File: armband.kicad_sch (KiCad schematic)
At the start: 14 parts, among them IC1 QSMP-1570, SW1 EVP-BB2A9B000, SW2 EVP-BB2A9B000

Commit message: progressed layout
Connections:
- net BMI_INT1: now also IC1.24 (ENET_RXC); no longer IC1.20 (ENET_CK125)
- net BMI_INT2: now also IC1.25 (ENET_RX_CTL); no longer IC1.21 (ENET_INT)
- net LCD_RST: now also IC1.20 (ENET_CK125); no longer IC1.26 (ENET_RXD0)
- net LCD_TE: now also IC1.19 (ENET_RST); no longer IC1.25 (ENET_RX_CTL)
- net MAX_INT: now also IC1.26 (ENET_RXD0); no longer IC1.22 (ENET_MDIO)
- net MP2722_INT: now also IC1.27 (ENET_RXD1); no longer IC1.19 (ENET_RST)
- net QSMP_LCD_EN: now also IC1.23 (ENET_MDC); no longer IC1.27 (ENET_RXD1)
- net TP_INT: now also IC1.21 (ENET_INT); no longer IC1.23 (ENET_MDC)
- net TP_RST: now also IC1.22 (ENET_MDIO); no longer IC1.24 (ENET_RXC)
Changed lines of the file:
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@@
     )
   )
-  (global_label "BMI_INT2" (shape input) (at 236.22 139.7 0) (fields_autoplaced)
-    (effects (font (size 1.27 1.27)) (justify left))
-    (property "Intersheetrefs" "${INTERSHEET_REFS}" (at 247.532 139.7 0)
+  (global_label "BMI_INT2" (shape input) (at 236.22 149.86 0) (fields_autoplaced)
+    (effects (font (size 1.27 1.27)) (justify left))
+    (property "Intersheetrefs" "${INTERSHEET_REFS}" (at 247.532 149.86 0)
       (effects (font (size 1.27 1.27)) (justify left) hide)
     )
@@
     )
   )
-  (global_label "TP_RST" (shape input) (at 236.22 147.32 0) (fields_autoplaced)
-    (effects (font (size 1.27 1.27)) (justify left))
-    (property "Intersheetrefs" "${INTERSHEET_REFS}" (at 245.7781 147.32 0)
+  (global_label "TP_RST" (shape input) (at 236.22 142.24 0) (fields_autoplaced)
+    (effects (font (size 1.27 1.27)) (justify left))
+    (property "Intersheetrefs" "${INTERSHEET_REFS}" (at 245.7781 142.24 0)
       (effects (font (size 1.27 1.27)) (justify left) hide)
     )
@@
     )
   )
-  (global_label "QSMP_LCD_EN" (shape input) (at 236.22 154.94 0) (fields_autoplaced)
-    (effects (font (size 1.27 1.27)) (justify left))
-    (property "Intersheetrefs" "${INTERSHEET_REFS}" (at 252.37 154.94 0)
+  (global_label "QSMP_LCD_EN" (shape input) (at 236.22 144.78 0) (fields_autoplaced)
+    (effects (font (size 1.27 1.27)) (justify left))
+    (property "Intersheetrefs" "${INTERSHEET_REFS}" (at 252.37 144.78 0)
       (effects (font (size 1.27 1.27)) (justify left) hide)
     )
@@
     )
   )
-  (global_label "MP2722_INT" (shape input) (at 236.22 134.62 0) (fields_autoplaced)
-    (effects (font (size 1.27 1.27)) (justify left))
-    (property "Intersheetrefs" "${INTERSHEET_REFS}" (at 250.5557 134.62 0)
+  (global_label "MP2722_INT" (shape input) (at 236.22 154.94 0) (fields_autoplaced)
+    (effects (font (size 1.27 1.27)) (justify left))
+    (property "Intersheetrefs" "${INTERSHEET_REFS}" (at 250.5557 154.94 0)
       (effects (font (size 1.27 1.27)) (justify left) hide)
     )
@@
     )
   )
-  (global_label "MAX_INT" (shape input) (at 236.22 142.24 0) (fields_autoplaced)
-    (effects (font (size 1.27 1.27)) (justify left))
-    (property "Intersheetrefs" "${INTERSHEET_REFS}" (at 246.7458 142.24 0)
+  (global_label "MAX_INT" (shape input) (at 236.22 152.4 0) (fields_autoplaced)
+    (effects (font (size 1.27 1.27)) (justify left))
+    (property "Intersheetrefs" "${INTERSHEET_REFS}" (at 246.7458 152.4 0)
       (effects (font (size 1.27 1.27)) (justify left) hide)
     )
@@
     )
   )
-  (global_label "BMI_INT1" (shape input) (at 236.22 137.16 0) (fields_autoplaced)
-    (effects (font (size 1.27 1.27)) (justify left))
-    (property "Intersheetrefs" "${INTERSHEET_REFS}" (at 247.532 137.16 0)
+  (global_label "BMI_INT1" (shape input) (at 236.22 147.32 0) (fields_autoplaced)
+    (effects (font (size 1.27 1.27)) (justify left))
+    (property "Intersheetrefs" "${INTERSHEET_REFS}" (at 247.532 147.32 0)
       (effects (font (size 1.27 1.27)) (justify left) hide)
     )
@@
     )
   )
-  (global_label "LCD_TE" (shape input) (at 236.22 149.86 0) (fields_autoplaced)
-    (effects (font (size 1.27 1.27)) (justify left))
-    (property "Intersheetrefs" "${INTERSHEET_REFS}" (at 245.7781 149.86 0)
+  (global_label "LCD_TE" (shape input) (at 236.22 134.62 0) (fields_autoplaced)
+    (effects (font (size 1.27 1.27)) (justify left))
+    (property "Intersheetrefs" "${INTERSHEET_REFS}" (at 245.7781 134.62 0)
       (effects (font (size 1.27 1.27)) (justify left) hide)
     )
@@
     )
   )
-  (global_label "LCD_RST" (shape input) (at 236.22 152.4 0) (fields_autoplaced)
-    (effects (font (size 1.27 1.27)) (justify left))
-    (property "Intersheetrefs" "${INTERSHEET_REFS}" (at 247.1086 152.4 0)
+  (global_label "LCD_RST" (shape input) (at 236.22 137.16 0) (fields_autoplaced)
+    (effects (font (size 1.27 1.27)) (justify left))
+    (property "Intersheetrefs" "${INTERSHEET_REFS}" (at 247.1086 137.16 0)
       (effects (font (size 1.27 1.27)) (justify left) hide)
     )
@@
     )
   )
-  (global_label "TP_INT" (shape input) (at 236.22 144.78 0) (fields_autoplaced)
-    (effects (font (size 1.27 1.27)) (justify left))
-    (property "Intersheetrefs" "${INTERSHEET_REFS}" (at 245.2339 144.78 0)
-      (effects (font (size 1.27 1.27)) (justify left) hide)
-    )
+  (global_label "TP_INT" (shape input) (at 236.22 139.7 0) (fields_autoplaced)
+    (effects (font (size 1.27 1.27)) (justify left))
+    (property "Intersheetrefs" "${INTERSHEET_REFS}" (at 245.2339 139.7 0)
+      (effects (font (size 1.27 1.27)) (justify left) hide)
+    )

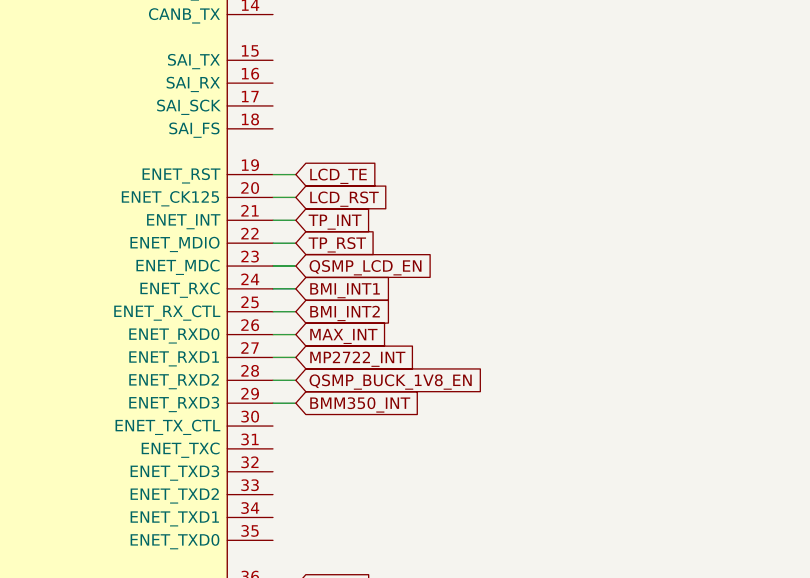
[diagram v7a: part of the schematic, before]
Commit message: progressed layout and made changes in bmi323 (set unconnected pins to NC) + changed debug connections in preparation to make bridges to debug part + changed VSYS, VUSB, VBAT+ and other connected power traces to 0.2mm trace thickness + added BMI323 layout + moved MAX30102 to make space for caps + added missing caps to MAX30102 + changed gpio order for better layout + added BMM350 layout next to BMI323
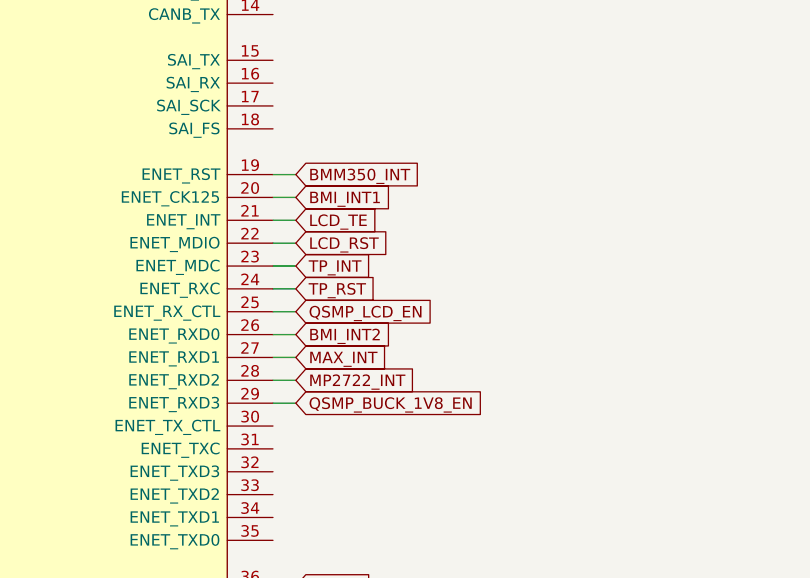
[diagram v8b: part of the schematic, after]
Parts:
- R1, R2, R3, R4: footprint Resistor_SMD:R_0201_0603Metric_Pad0.64x0.40mm_HandSolder -> Resistor_SMD:R_0201_0603Metric
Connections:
- net BMI_INT1: now also IC1.20 (ENET_CK125); no longer IC1.24 (ENET_RXC)
- net BMI_INT2: now also IC1.26 (ENET_RXD0); no longer IC1.25 (ENET_RX_CTL)
- net BMM350_INT: now also IC1.19 (ENET_RST); no longer IC1.29 (ENET_RXD3)
- net LCD_RST: now also IC1.22 (ENET_MDIO); no longer IC1.20 (ENET_CK125)
- net LCD_TE: now also IC1.21 (ENET_INT); no longer IC1.19 (ENET_RST)
- net MAX_INT: now also IC1.27 (ENET_RXD1); no longer IC1.26 (ENET_RXD0)
- net MP2722_INT: now also IC1.28 (ENET_RXD2); no longer IC1.27 (ENET_RXD1)
- net QSMP_BUCK_1V8_EN: now also IC1.29 (ENET_RXD3); no longer IC1.28 (ENET_RXD2)
- net QSMP_LCD_EN: now also IC1.25 (ENET_RX_CTL); no longer IC1.23 (ENET_MDC)
- net TP_INT: now also IC1.23 (ENET_MDC); no longer IC1.21 (ENET_INT)
- net TP_RST: now also IC1.24 (ENET_RXC); no longer IC1.22 (ENET_MDIO)
